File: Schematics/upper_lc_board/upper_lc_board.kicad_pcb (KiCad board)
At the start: 4 copper layers, 69.5 x 60 mm, 111 parts, among them J1 Stack Male Edge Connector, J2 SOL_CONN, J3 PT2, J4 PT1, J5 HALL, J6 SOL2_CONN, J7 TC, J8 USB_C_Female_USB2_Small, Q1 AO3400A, Q2 AO3400A, SW1 SW_ESP_BOOT_MODE, SW2 SW_ESP_RESET, U1 ESP32-S3-WROOM-1-N16, U2 ISO1044BDR, U3 AMS1117-3.3, U4 ID_LM66100DCKR, U5 ID_LM66100DCKR, U6 LM324DT, U7 ADC_ADS131M04IPWR

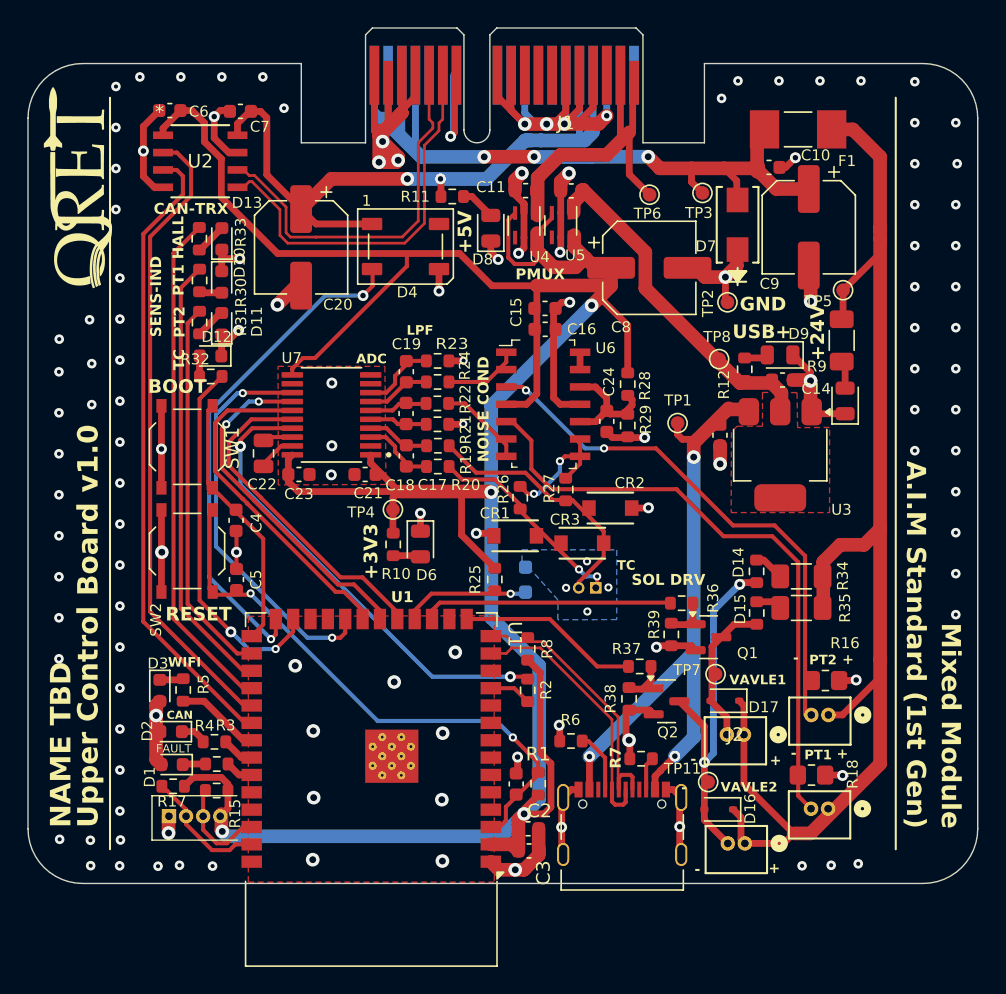
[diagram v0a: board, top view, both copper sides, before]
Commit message: updated opamp, 24v tvs diode, and excluded usbc antenna overlap error
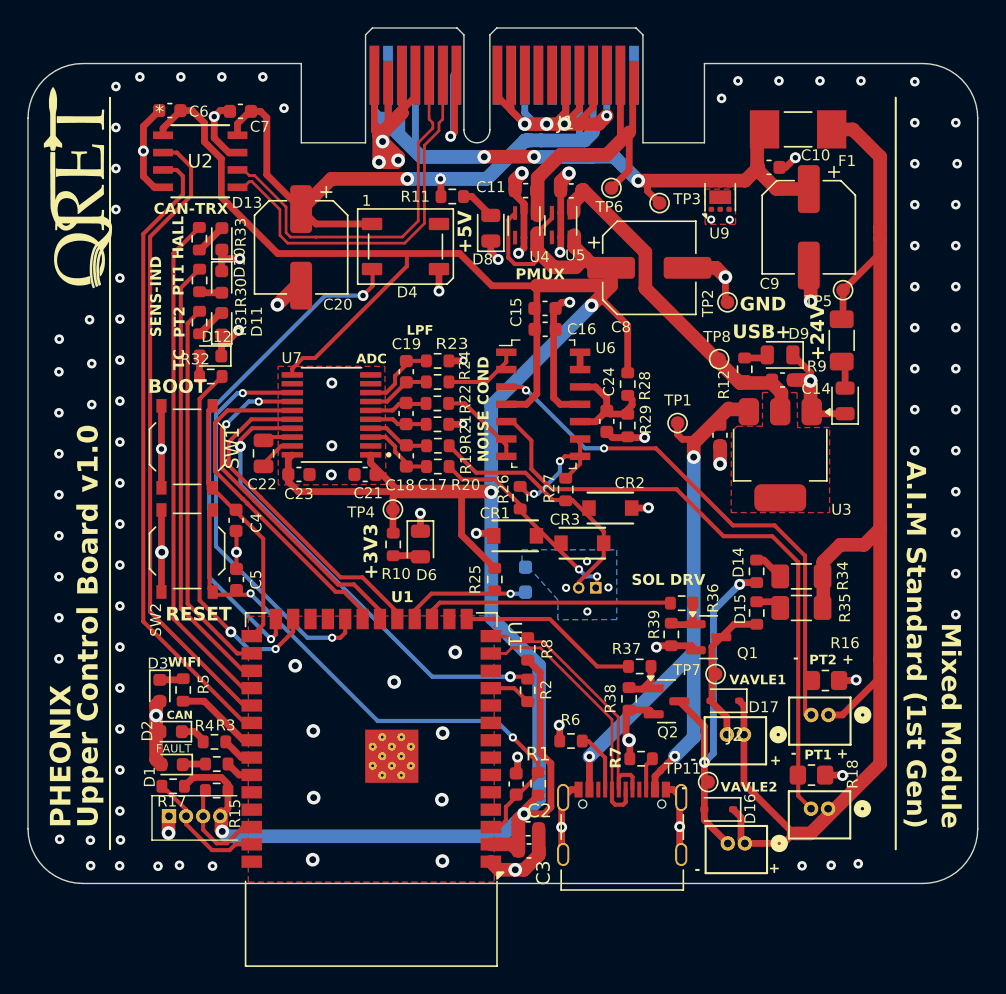
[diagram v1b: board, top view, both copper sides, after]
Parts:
- removed D7: D_TVS, SMA6L30A:SMASeries_LTF-L
- added U9: TVS3300DRV, Package_SON:WSON-6-1EP_2x2mm_P0.65mm_EP1x1.6mm, F.Cu at (146.1, 76.2)
- U6: value LM324DT -> TSV914
- moved TP3 3.23 mm to (141.7, 76.6)
- moved TP6 2.83 mm to (138.1, 75.5)
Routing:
- net GND: track 214.5 -> 212.1 mm, vias 135 -> 137
- net +24V_BP: track 66.6 -> 64.5 mm
- net /Power Circuitry/3V3_BP: track 24.8 -> 24.3 mm
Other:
- board text added: "PHEONIX"
- board text removed: "NAME TBD"

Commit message: fixed valve FB diode footprints, fixed major silkscreen warnings
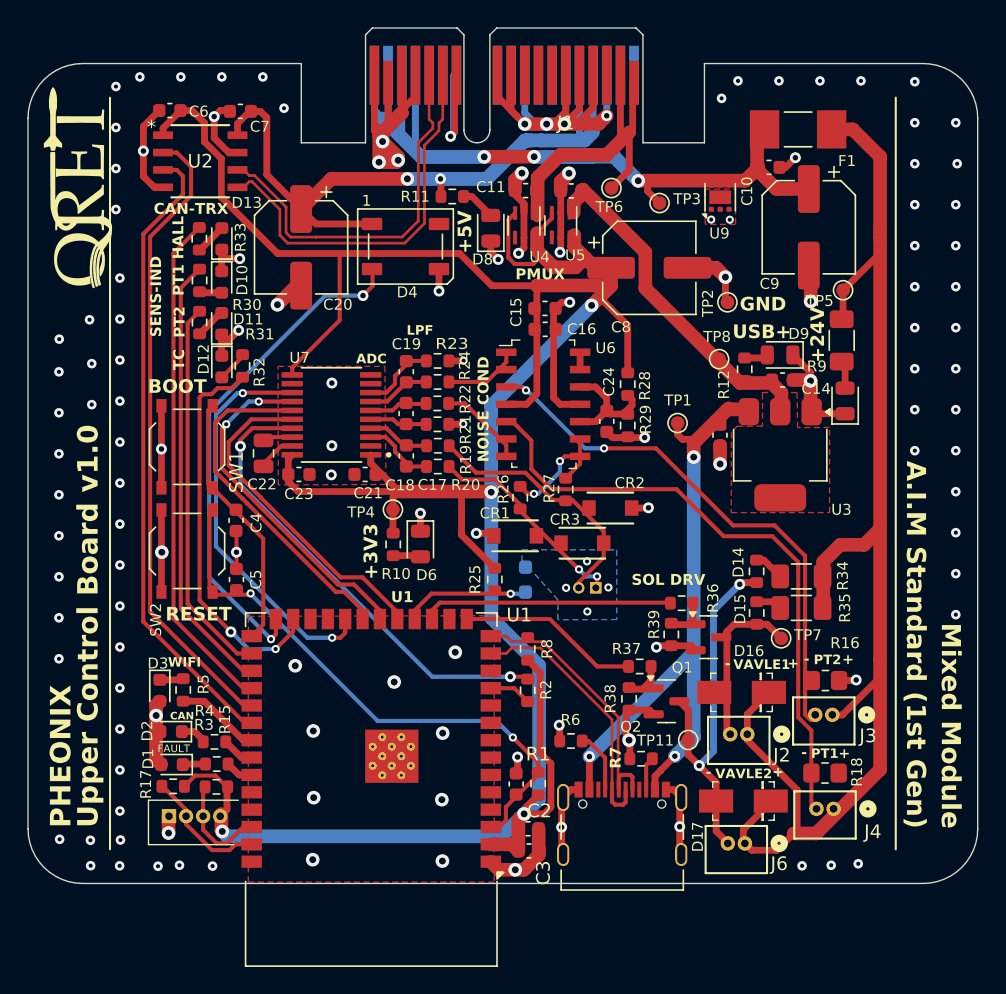
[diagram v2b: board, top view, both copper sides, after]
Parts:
- D16, D17: value D_FB -> SS14; footprint Diode_SMD:D_SOD-323 -> digikey-footprints:DO-214AC
- moved D16 8.72 mm to (147.7, 112.4)
- moved D17 7.47 mm to (147.8, 120.3)
- moved TP7 5.47 mm to (150.6, 108.4)
- moved TP11 3.41 mm to (143.8, 115.9)
- moved R32 2.44 mm to (111.1, 88.5), turned to 90 degrees
- moved D12 1.14 mm to (109.6, 88.6), turned to -90 degrees
- moved R18 1.00 mm to (153.8, 118.3)
- moved J4 0.40 mm to (154.4, 120.9)
- moved J3 0.29 mm to (154.3, 114.0)
- moved R15 0.27 mm to (109.2, 119.3)
- moved J2 0.25 mm to (148.1, 115.5)
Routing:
- net +3V3: track 217.7 -> 215.0 mm
- net +24V: track 97.6 -> 100.1 mm
- net TC_LED: track 26.8 -> 28.4 mm
- net GND: track 212.1 -> 210.8 mm, vias 137 -> 136
- net SOL1_RET: track 10.9 -> 12.2 mm
- net Net-(D12-A): track 1.51 -> 2.29 mm

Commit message: updates after review using screw terminal for TC removed opamps for clamping diodes fixed solenoid FB diodes manual solder large SMDs on edges
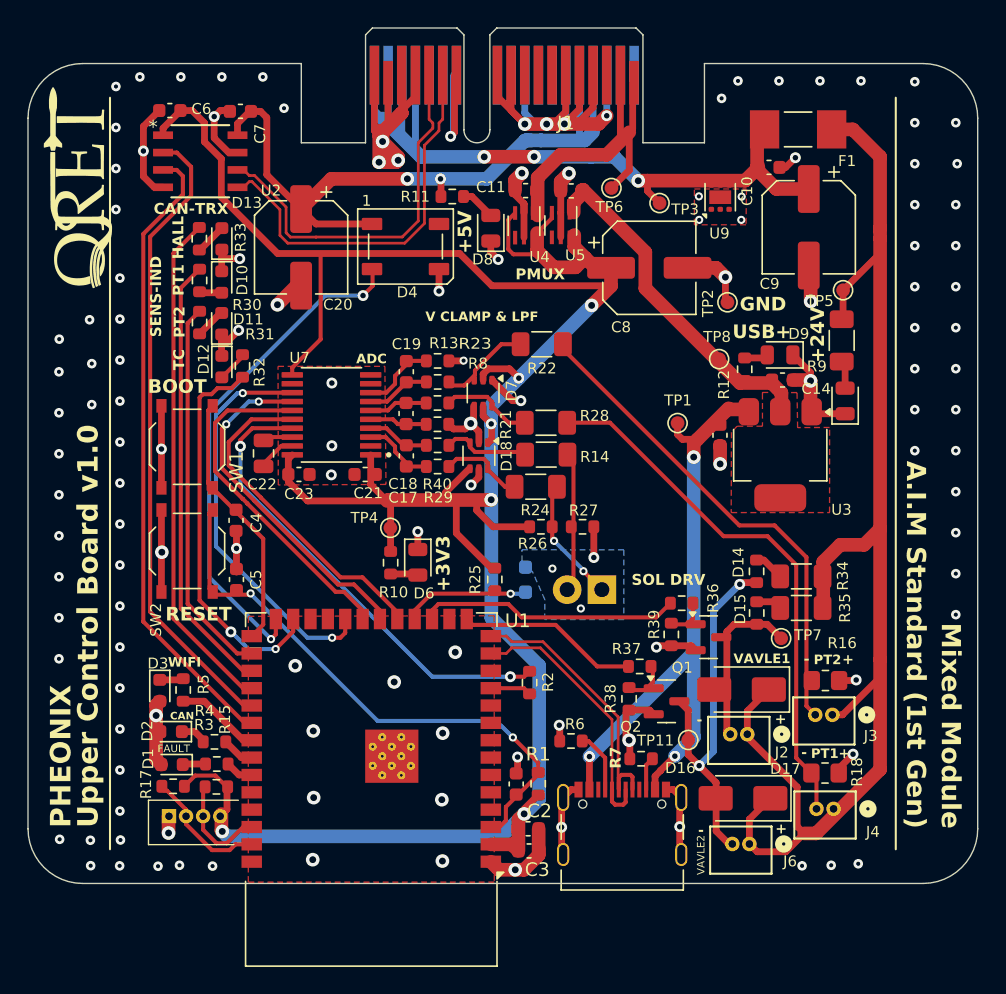
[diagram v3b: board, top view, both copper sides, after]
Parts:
- removed C15: 10uF, Capacitor_SMD:C_0603_1608Metric
- removed C16, C24: 0.1uF, Capacitor_SMD:C_0603_1608Metric
- removed CR1, CR2, CR3: SMF15CA, SMF5_0CA:SOD-123F_LTF-L
- removed R19, R20: 1k, Resistor_SMD:R_0603_1608Metric
- removed U6: TSV914, digikey-footprints:SOIC-14_W3.9mm
- added D18: BAV199DW, Package_TO_SOT_SMD:SOT-363_SC-70-6, F.Cu at (128.4, 95.1)
- added D7: BAV199DW, Package_TO_SOT_SMD:SOT-363_SC-70-6, F.Cu at (128.8, 90.5)
- added R13: 200, Resistor_SMD:R_0603_1608Metric, F.Cu at (125.4, 91.2)
- added R14: 1k, Resistor_SMD:R_1206_3216Metric_Pad1.30x1.75mm_HandSolder, F.Cu at (133.3, 92.7)
- added R40: 200, Resistor_SMD:R_0603_1608Metric, F.Cu at (125.4, 94.3)
- D16, D17: value SS14 -> SS34; footprint digikey-footprints:DO-214AC -> Diode_SMD:D_SMA
- J2: value SOL_CONN -> SOL1_CONN
- J7: value TC -> Screw_Terminal_01x02; footprint 530480210:MOLEX_530480210 -> TerminalBlock_TE-Connectivity:TerminalBlock_TE_282834-2_1x02_P2.54mm_Horizontal
- R21, R23: value 1k -> 1.2k
- R22, R24: footprint Resistor_SMD:R_0603_1608Metric -> Resistor_SMD:R_1206_3216Metric_Pad1.30x1.75mm_HandSolder
- R28: value 10k -> 1k; footprint Resistor_SMD:R_0603_1608Metric -> Resistor_SMD:R_1206_3216Metric_Pad1.30x1.75mm_HandSolder
- R29: value 10k -> 200
- R8: value 1.5k -> 200
- moved R8 20.6 mm to (125.4, 89.7), turned to 0 degrees
- moved R29 14.2 mm to (125.4, 95.9), turned to 180 degrees
- moved R24 10.5 mm to (132.6, 97.3), turned to 0 degrees
- moved R22 8.78 mm to (133.0, 86.9)
- moved R28 7.88 mm to (133.4, 95.0), turned to 0 degrees
- moved R27 2.99 mm to (136.0, 100.3), turned to 0 degrees
- moved R26 2.62 mm to (133.0, 100.3), turned to 0 degrees
- moved TP4 1.35 mm to (122.0, 100.4)
- moved D6 1.35 mm to (124.0, 102.9)
- moved R10 1.35 mm to (122.0, 102.9)
- moved R2 0.59 mm to (132.2, 111.7)
- moved J7 0.46 mm to (137.4, 104.9)
- moved J6 0.33 mm to (148.2, 123.5)
- moved D16 0.21 mm to (147.7, 112.2)
- moved D17 0.20 mm to (147.8, 120.2)
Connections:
- net Net-(J4-Pin_2) renamed /Sensor Circuitry/PT1
- net Net-(U7-AIN0N) renamed /Sensor Circuitry/TC_N_CLAMPED
- C17 pad 2: Net-(U7-AIN0P) -> /Sensor Circuitry/TC_P_CLAMPED
- C18 pad 2: Net-(U7-AIN1P) -> /Sensor Circuitry/PT1_CLAMPED
- C19 pad 2: Net-(U7-AIN2P) -> /Sensor Circuitry/PT2_CLAMPED
- J3 pad 2: Net-(J3-Pin_2) -> /Sensor Circuitry/PT2
- R16 pad 2: Net-(J3-Pin_2) -> /Sensor Circuitry/PT2
- R22 pad 1: /Sensor Circuitry/PT2_OUT -> /Sensor Circuitry/PT2
- R22 pad 2: Net-(U7-AIN1P) -> Net-(D7B-K1A2)
- R24 pad 1: /Sensor Circuitry/PT1_OUT -> Net-(D18A-K3A4)
- R24 pad 2: Net-(U7-AIN2P) -> /Sensor Circuitry/TC_P
- R26 pad 1: /Sensor Circuitry/VMID -> +3V3
- R27 pad 2: /Sensor Circuitry/VMID -> GND
- R28 pad 1: +3V3 -> Net-(D18B-K1A2)
- R28 pad 2: /Sensor Circuitry/V_DIVIDER -> /Sensor Circuitry/TC_N
- R29 pad 1: /Sensor Circuitry/V_DIVIDER -> Net-(D18A-K3A4)
- R29 pad 2: GND -> /Sensor Circuitry/TC_P_CLAMPED
- R8 pad 1: /ESP Breakout Cirucitry/USB_P -> /Sensor Circuitry/PT2_CLAMPED
- R8 pad 2: +3V3 -> Net-(D7B-K1A2)
- U7 pad 3: Net-(U7-AIN0P) -> /Sensor Circuitry/TC_P_CLAMPED
- U7 pad 6: Net-(U7-AIN1P) -> /Sensor Circuitry/PT1_CLAMPED
- U7 pad 7: Net-(U7-AIN2P) -> /Sensor Circuitry/PT2_CLAMPED
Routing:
- net Net-(J3-Pin_2): track 39.2 -> 0.00 mm, vias 2 -> 0
- net /Sensor Circuitry/PT2: track 0.00 -> 36.3 mm
- net +3V3: track 215.0 -> 197.7 mm, vias 4 -> 6
- net /Sensor Circuitry/VMID: track 9.52 -> 0.00 mm, vias 2 -> 0
- net /Sensor Circuitry/V_DIVIDER: track 8.55 -> 0.00 mm
- net /Sensor Circuitry/TC_N: track 18.8 -> 10.7 mm
- net Net-(D7B-K1A2): track 0.00 -> 6.79 mm
- net Net-(D18B-K1A2): track 0.00 -> 6.78 mm
- net Net-(D7A-K3A4): track 0.00 -> 6.40 mm
- net /Sensor Circuitry/PT2_OUT: track 6.31 -> 0.00 mm
- net Net-(D18A-K3A4): track 0.00 -> 6.17 mm
- net GND: track 210.8 -> 204.9 mm, vias 136 -> 134
- net /Sensor Circuitry/TC_P: track 15.3 -> 9.62 mm
- net /Sensor Circuitry/PT1_OUT: track 5.52 -> 0.00 mm
- net /Sensor Circuitry/PT1: track 45.3 -> 39.8 mm
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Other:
- board text added: "V CLAMP & LPF"
- board text removed: "LPF"
- board text removed: "NOISE COND"
- board text removed: "U1"

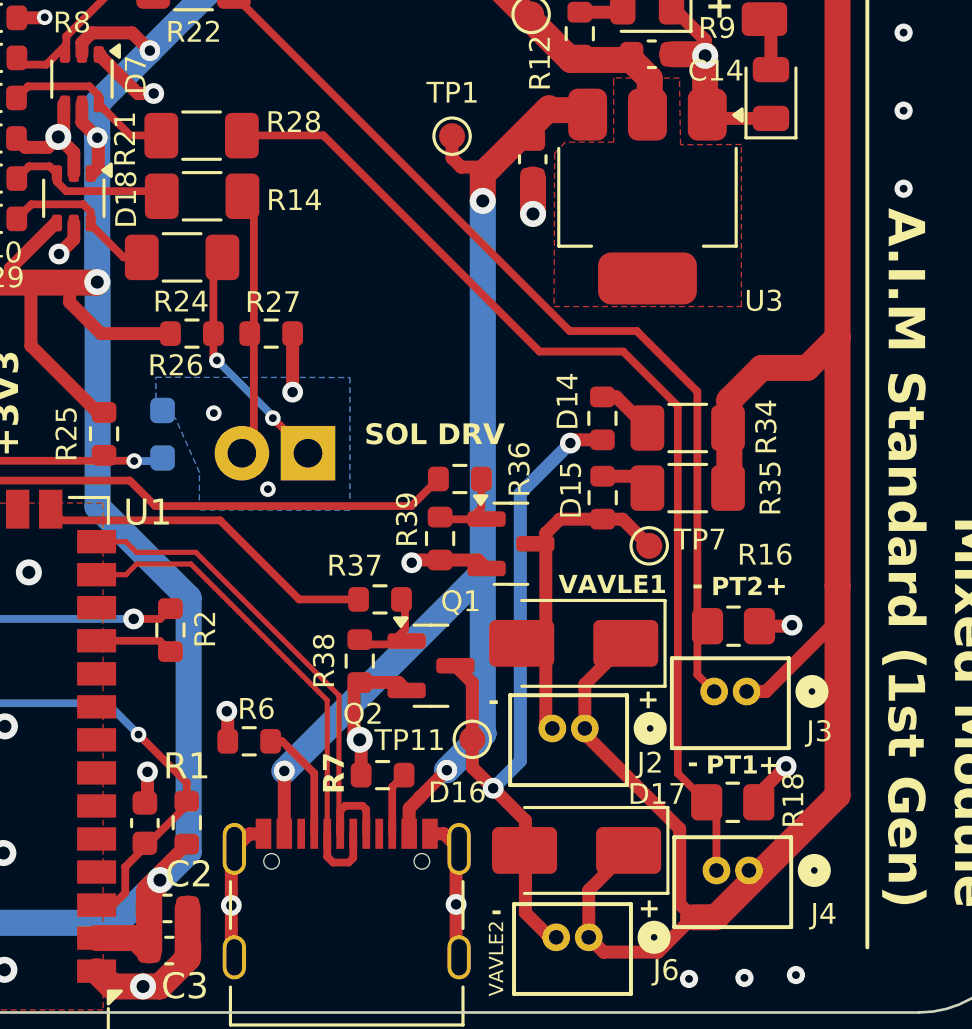
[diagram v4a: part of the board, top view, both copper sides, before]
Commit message: add hierarchy sheet blocks for valve, TC & PT circuitry.
confirmed that nets are consistent with layout, no problems.
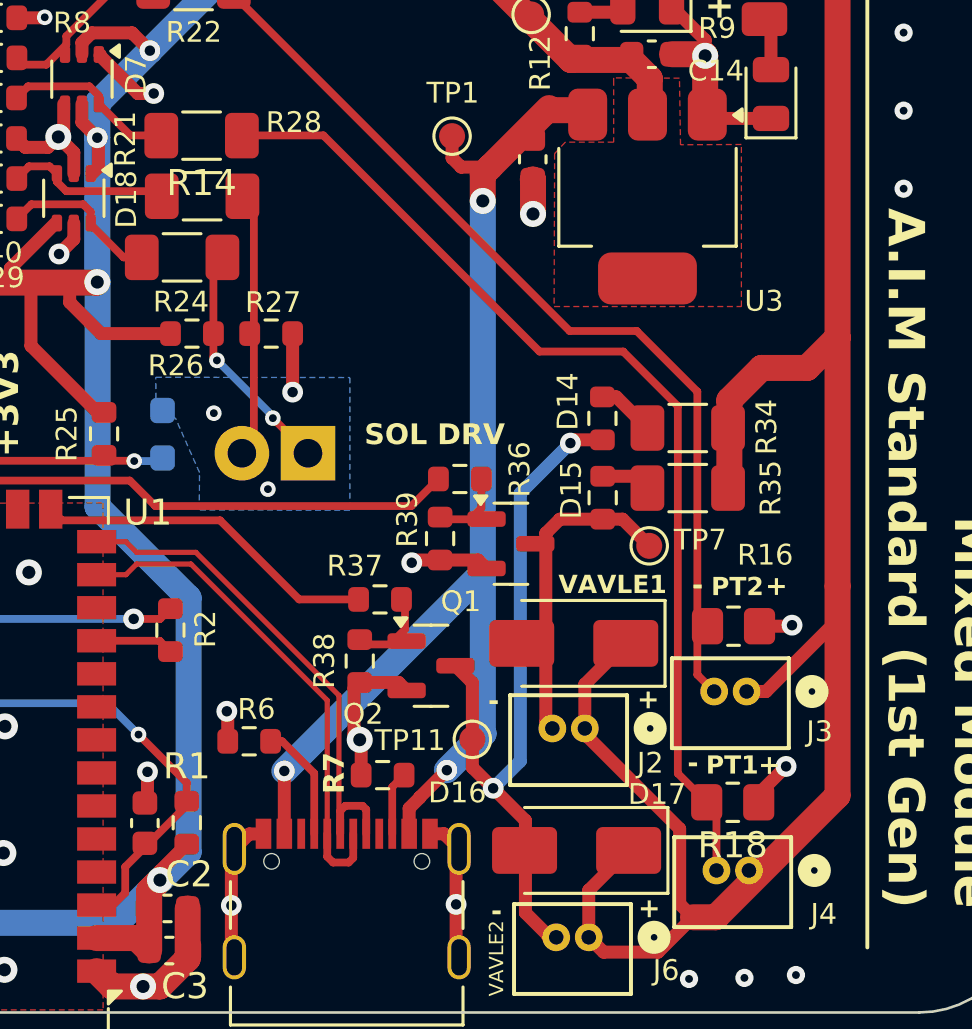
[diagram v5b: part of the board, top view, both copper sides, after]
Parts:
- J3: value PT2 -> PT1

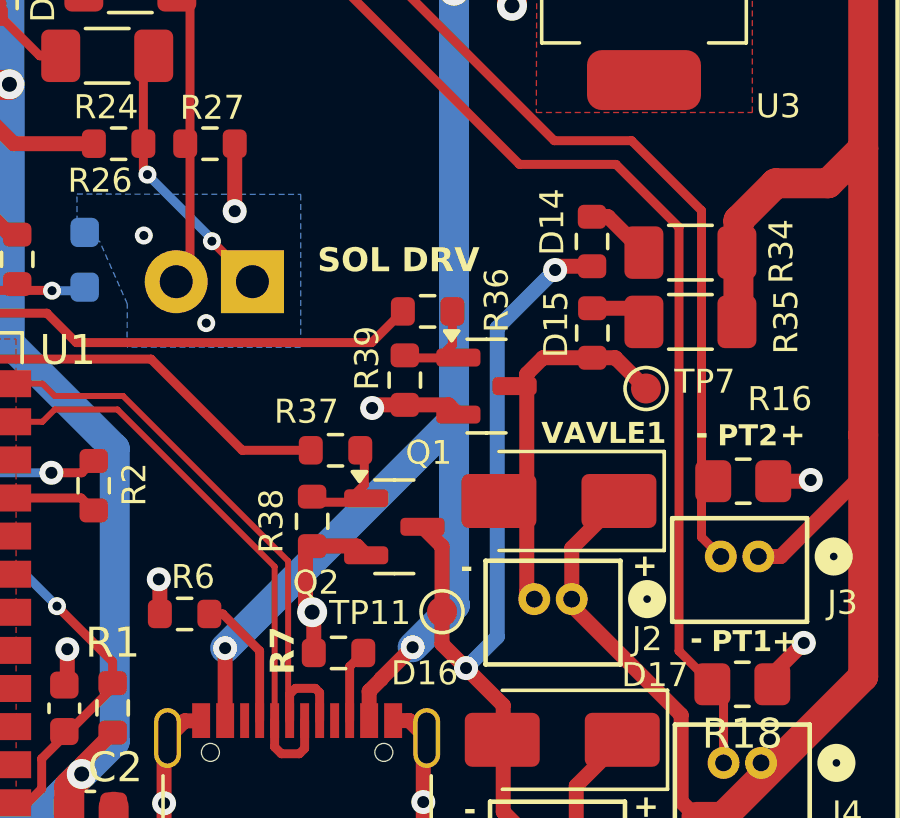
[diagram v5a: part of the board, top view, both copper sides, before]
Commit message: matched pcb silk to fabricated one
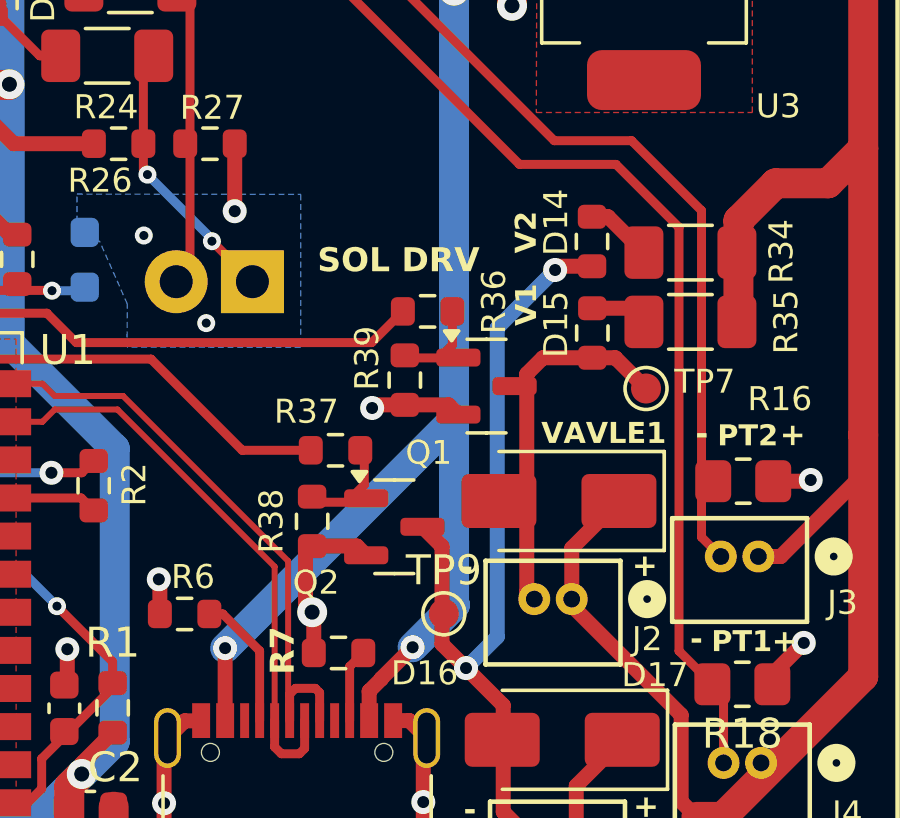
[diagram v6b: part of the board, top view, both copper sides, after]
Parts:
- removed TP11: VALVE2_OUT_TP, TestPoint:TestPoint_Pad_D1.0mm
- added TP9: VALVE2_OUT_TP, TestPoint:TestPoint_Pad_D1.0mm, F.Cu at (143.8, 116.0)
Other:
- board text added: "V1"
- board text added: "V2"

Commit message: add references to caps, ferrite bead footprint, LDO datasheet
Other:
- board text added: "Pheonix V1.0 QRET Dec 2025 Jeevan Sanchez Tristan Alderson"
- board text removed: "____________ V1.0 QRET Dec 2025 Jeevan Sanchez Tristan Alderson"
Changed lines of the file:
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@@
 		)
 	)
-	(gr_text "____________ V1.0\nQRET Dec 2025\n\nJeevan Sanchez\nTristan Alderson\n"
+	(gr_text "Pheonix V1.0\nQRET Dec 2025\n\nJeevan Sanchez\nTristan Alderson\n"
 		(at 129.78 76.69 0)
 		(layer "B.SilkS")
